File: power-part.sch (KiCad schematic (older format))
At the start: 6 parts, among them P5 5V, P6 8..24V, U8 MC7805CDTG

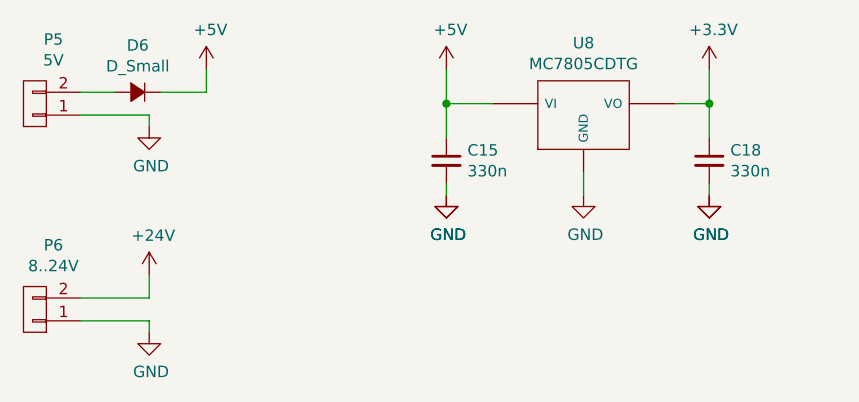
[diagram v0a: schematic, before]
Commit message: schematic seems ok, ongoing routing
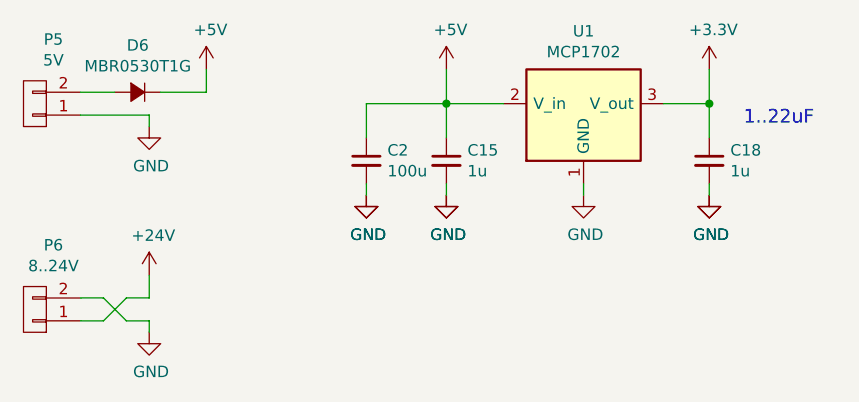
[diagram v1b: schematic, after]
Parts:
- removed U8: MC7805CDTG, TO_SOT_Packages_SMD:SOT-428, symbol 7805
- added C2: 100u, Capacitors_SMD:c_elec_6.3x4.5, symbol C_Small
- added U1: MCP1702, TO_SOT_Packages_SMD:SOT89-3_Housing, symbol MCP1702
- C15, C18: value 330n -> 1u; footprint Capacitors_SMD:C_1206 -> Capacitors_SMD:C_0805
- D6: value D_Small -> MBR0530T1G; footprint TO_SOT_Packages_SMD:SOT-23 -> Diodes_SMD:SOD-123
- P5, P6: footprint Sockets_MOLEX_KK-System:Socket_MOLEX-KK-RM3-96mm_Lock_2pin_straight -> Connect:JWT_Vertical_A3963-RM3.96mm-2
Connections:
- net +24V: now also P6.1 (P1); no longer P6.2 (P2)
- net +3V3: now also U1.3 (V_out)
- net +5V: now also C2.1, U1.2 (V_in)
- net GND: now also P6.2 (P2), C2.2, U1.1 (GND); no longer P6.1 (P1)
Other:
- note added: "1..22uF"
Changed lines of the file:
@@
 $Descr A4 11693 8268
 encoding utf-8
-Sheet 6 7
+Sheet 6 9
 Title ""
 Date ""
@@
 $EndDescr
 $Comp
-L GND #PWR049
+L GND #PWR58
 U 1 1 5705D661
 P 4950 1800
-F 0 "#PWR049" H 4950 1550 50  0001 C CNN
+F 0 "#PWR58" H 4950 1550 50  0001 C CNN
 F 1 "GND" H 4958 1627 50  0000 C CNN
 F 2 "" H 4950 1800 50  0000 C CNN
@@
 $EndComp
 Wire Wire Line
-	4950 1800 4950 1700
-Wire Wire Line
-	4350 1400 4550 1400
-Wire Wire Line
 	4350 1250 4350 1550
 $Comp
-L GND #PWR050
+L GND #PWR56
 U 1 1 5705D671
 P 4350 1800
-F 0 "#PWR050" H 4350 1550 50  0001 C CNN
+F 0 "#PWR56" H 4350 1550 50  0001 C CNN
 F 1 "GND" H 4358 1627 50  0000 C CNN
 F 2 "" H 4350 1800 50  0000 C CNN
@@
 	4350 1800 4350 1750
 Wire Wire Line
-	5350 1400 5500 1400
-Wire Wire Line
 	5500 1250 5500 1550
 Connection ~ 4350 1400
-$Comp
-L 7805 U8
-U 1 1 5705D687
-P 4950 1450
-F 0 "U8" H 4950 1765 50  0000 C CNN
-F 1 "MC7805CDTG" H 4950 1674 50  0000 C CNN
-F 2 "TO_SOT_Packages_SMD:SOT-428" H 4950 1450 50  0001 C CNN
-F 3 "" H 4950 1450 50  0000 C CNN
-	1    4950 1450
-	1    0    0    -1
-$EndComp
 $Comp
 L C_Small C15
@@
 P 4350 1650
 F 0 "C15" H 4442 1696 50  0000 L CNN
-F 1 "330n" H 4442 1605 50  0000 L CNN
-F 2 "Capacitors_SMD:C_1206" H 4350 1650 50  0001 C CNN
+F 1 "1u" H 4442 1605 50  0000 L CNN
+F 2 "Capacitors_SMD:C_0805" H 4350 1650 50  0001 C CNN
 F 3 "" H 4350 1650 50  0000 C CNN
 	1    4350 1650
@@
 $EndComp
 $Comp
-L GND #PWR051
+L GND #PWR57
 U 1 1 5705D694
 P 4350 1800
-F 0 "#PWR051" H 4350 1550 50  0001 C CNN
+F 0 "#PWR57" H 4350 1550 50  0001 C CNN
 F 1 "GND" H 4358 1627 50  0000 C CNN
 F 2 "" H 4350 1800 50  0000 C CNN
@@
 $EndComp
 $Comp
-L GND #PWR052
+L GND #PWR60
 U 1 1 5705D6A3
 P 5500 1800
-F 0 "#PWR052" H 5500 1550 50  0001 C CNN
+F 0 "#PWR60" H 5500 1550 50  0001 C CNN
 F 1 "GND" H 5508 1627 50  0000 C CNN
 F 2 "" H 5500 1800 50  0000 C CNN
@@
 P 5500 1650
 F 0 "C18" H 5592 1696 50  0000 L CNN
-F 1 "330n" H 5592 1605 50  0000 L CNN
-F 2 "Capacitors_SMD:C_1206" H 5500 1650 50  0001 C CNN
+F 1 "1u" H 5592 1605 50  0000 L CNN
+F 2 "Capacitors_SMD:C_0805" H 5500 1650 50  0001 C CNN
 F 3 "" H 5500 1650 50  0000 C CNN
 	1    5500 1650
@@
 $EndComp
 $Comp
-L GND #PWR053
+L GND #PWR61
 U 1 1 5705D6B2
 P 5500 1800
-F 0 "#PWR053" H 5500 1550 50  0001 C CNN
+F 0 "#PWR61" H 5500 1550 50  0001 C CNN
 F 1 "GND" H 5508 1627 50  0000 C CNN
 F 2 "" H 5500 1800 50  0000 C CNN
@@
 $EndComp
 $Comp
-L +5V #PWR054
+L +5V #PWR55
 U 1 1 5705D6E2
 P 4350 1250
-F 0 "#PWR054" H 4350 1100 50  0001 C CNN
+F 0 "#PWR55" H 4350 1100 50  0001 C CNN
 F 1 "+5V" H 4368 1423 50  0000 C CNN
 F 2 "" H 4350 1250 50  0000 C CNN
@@
 $EndComp
 $Comp
-L +3.3V #PWR055
+L +3.3V #PWR59
 U 1 1 5705D6F7
 P 5500 1250
-F 0 "#PWR055" H 5500 1100 50  0001 C CNN
+F 0 "#PWR59" H 5500 1100 50  0001 C CNN
 F 1 "+3.3V" H 5518 1423 50  0000 C CNN
 F 2 "" H 5500 1250 50  0000 C CNN
@@
 F 0 "P6" H 2469 2019 50  0000 C CNN
 F 1 "8..24V" H 2469 2110 50  0000 C CNN
-F 2 "Sockets_MOLEX_KK-System:Socket_MOLEX-KK-RM3-96mm_Lock_2pin_straight" H 2550 2300 50  0001 C CNN
+F 2 "Connect:JWT_Vertical_A3963-RM3.96mm-2" H 2550 2300 50  0001 C CNN
 F 3 "" H 2550 2300 50  0000 C CNN
 	1    2550 2300
@@
 $EndComp
 $Comp
-L +24V #PWR056
+L +24V #PWR50
 U 1 1 5705DF9A
 P 3050 2150
-F 0 "#PWR056" H 3050 2000 50  0001 C CNN
+F 0 "#PWR50" H 3050 2000 50  0001 C CNN
 F 1 "+24V" H 3068 2323 50  0000 C CNN
 F 2 "" H 3050 2150 50  0000 C CNN
@@
 $EndComp
 Wire Wire Line
-	2750 2250 3050 2250
-Wire Wire Line
 	3050 2250 3050 2150
 $Comp
-L GND #PWR057
+L GND #PWR51
 U 1 1 5705E164
 P 3050 2400
-F 0 "#PWR057" H 3050 2150 50  0001 C CNN
+F 0 "#PWR51" H 3050 2150 50  0001 C CNN
 F 1 "GND" H 3058 2227 50  0000 C CNN
 F 2 "" H 3050 2400 50  0000 C CNN
@@
 Wire Wire Line
 	3050 2400 3050 2350
-Wire Wire Line
-	3050 2350 2750 2350
 $Comp
 L CONN_01X02 P5
@@
 F 0 "P5" H 2469 1119 50  0000 C CNN
 F 1 "5V" H 2469 1210 50  0000 C CNN
-F 2 "Sockets_MOLEX_KK-System:Socket_MOLEX-KK-RM3-96mm_Lock_2pin_straight" H 2550 1400 50  0001 C CNN
+F 2 "Connect:JWT_Vertical_A3963-RM3.96mm-2" H 2550 1400 50  0001 C CNN
 F 3 "" H 2550 1400 50  0000 C CNN
 	1    2550 1400
@@
 	3300 1350 3300 1250
 $Comp
-L GND #PWR058
+L GND #PWR49
 U 1 1 57066A55
 P 3050 1500
-F 0 "#PWR058" H 3050 1250 50  0001 C CNN
+F 0 "#PWR49" H 3050 1250 50  0001 C CNN
 F 1 "GND" H 3058 1327 50  0000 C CNN
 F 2 "" H 3050 1500 50  0000 C CNN
@@
 	3050 1450 2750 1450
 $Comp
-L +5V #PWR059
+L +5V #PWR52
 U 1 1 57066A78
 P 3300 1250
-F 0 "#PWR059" H 3300 1100 50  0001 C CNN
+F 0 "#PWR52" H 3300 1100 50  0001 C CNN
 F 1 "+5V" H 3318 1423 50  0000 C CNN
 F 2 "" H 3300 1250 50  0000 C CNN
@@
 P 3000 1350
 F 0 "D6" H 3000 1145 50  0000 C CNN
-F 1 "D_Small" H 3000 1236 50  0000 C CNN
-F 2 "TO_SOT_Packages_SMD:SOT-23" V 3000 1350 50  0001 C CNN
+F 1 "MBR0530T1G" H 3000 1236 50  0000 C CNN
+F 2 "Diodes_SMD:SOD-123" V 3000 1350 50  0001 C CNN
 F 3 "" V 3000 1350 50  0000 C CNN
 	1    3000 1350
@@
 Wire Wire Line
 	3100 1350 3300 1350
+Text Notes 5650 1500 0    60   ~ 0
+1..22uF
+$Comp
+L GND #PWR53
+U 1 1 57070DDF
+P 4000 1800
+F 0 "#PWR53" H 4000 1550 50  0001 C CNN
+F 1 "GND" H 4008 1627 50  0000 C CNN
+F 2 "" H 4000 1800 50  0000 C CNN
+F 3 "" H 4000 1800 50  0000 C CNN
+	1    4000 1800
+	1    0    0    -1
+$EndComp
+Wire Wire Line
+	4000 1800 4000 1750
+$Comp
+L C_Small C2
+U 1 1 57070DE6
+P 4000 1650
+F 0 "C2" H 4092 1696 50  0000 L CNN
+F 1 "100u" H 4092 1605 50  0000 L CNN
+F 2 "Capacitors_SMD:c_elec_6.3x4.5" H 4000 1650 50  0001 C CNN
+F 3 "" H 4000 1650 50  0000 C CNN
+	1    4000 1650
+	1    0    0    -1
+$EndComp
+$Comp
+L GND #PWR54
+U 1 1 57070DEC
+P 4000 1800
+F 0 "#PWR54" H 4000 1550 50  0001 C CNN
+F 1 "GND" H 4008 1627 50  0000 C CNN
+F 2 "" H 4000 1800 50  0000 C CNN
+F 3 "" H 4000 1800 50  0000 C CNN
+	1    4000 1800
+	1    0    0    -1
+$EndComp
+Wire Wire Line
+	4000 1400 4000 1550
+Wire Wire Line
+	2750 2250 2850 2250
+Wire Wire Line
+	2850 2250 2950 2350
+Wire Wire Line
+	2750 2350 2850 2350
+Wire Wire Line
+	2850 2350 2950 2250
+Wire Wire Line
+	2950 2250 3050 2250
+Wire Wire Line
+	2950 2350 3050 2350
+$Comp
+L MCP1702 U1
+U 1 1 57088AC7
+P 4950 1450
+F 0 "U1" H 4950 1817 50  0000 C CNN
+F 1 "MCP1702" H 4950 1726 50  0000 C CNN
+F 2 "TO_SOT_Packages_SMD:SOT89-3_Housing" H 4950 1450 50  0001 C CNN
+F 3 "" H 4950 1450 50  0000 C CNN
+	1    4950 1450
+	1    0    0    -1
+$EndComp
+Wire Wire Line
+	4950 1800 4950 1750
+Wire Wire Line
+	5500 1400 5300 1400
+Wire Wire Line
+	4000 1400 4600 1400
 $EndSCHEMATC
